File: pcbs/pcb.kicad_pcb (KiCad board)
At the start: 2 copper layers, 148.3 x 111.7 mm, 54 parts

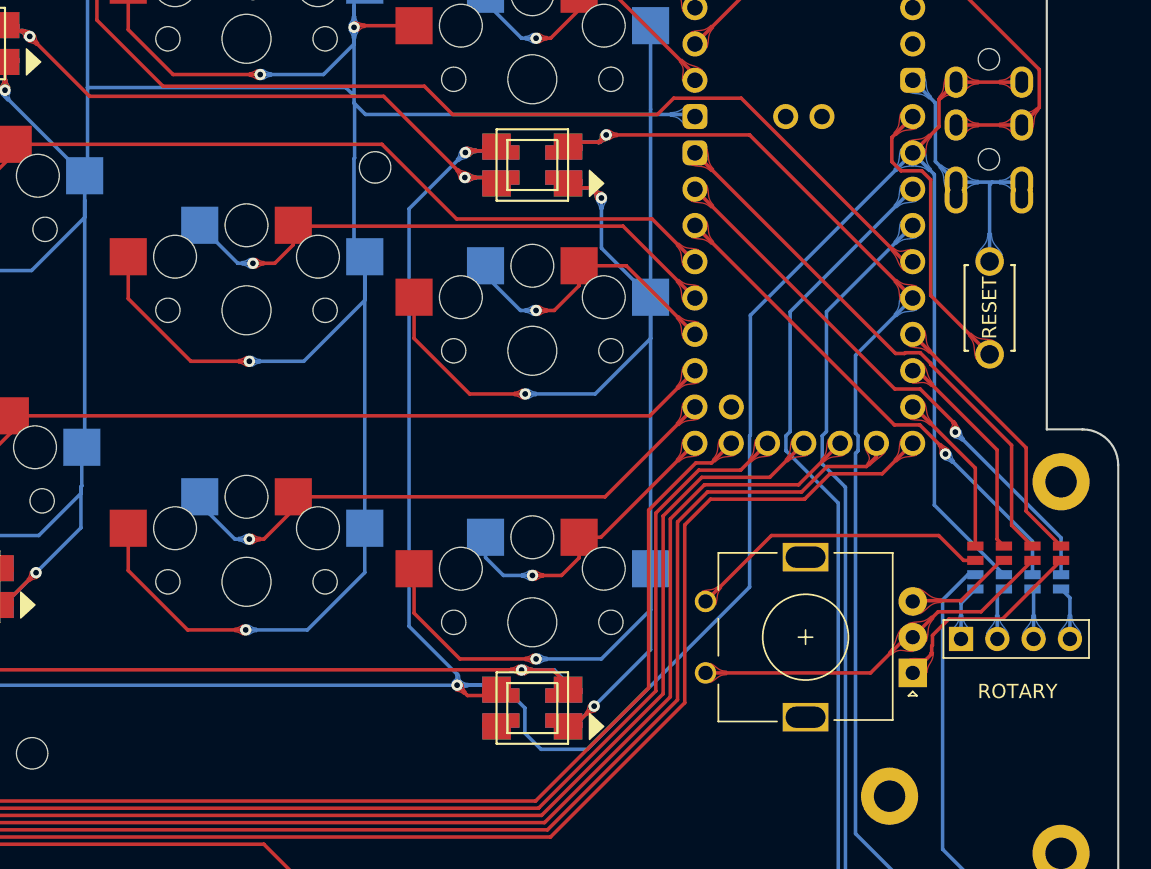
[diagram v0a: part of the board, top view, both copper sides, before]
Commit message: Connect LEDs' VDD pin to Helios' RGB pin for stable 5V
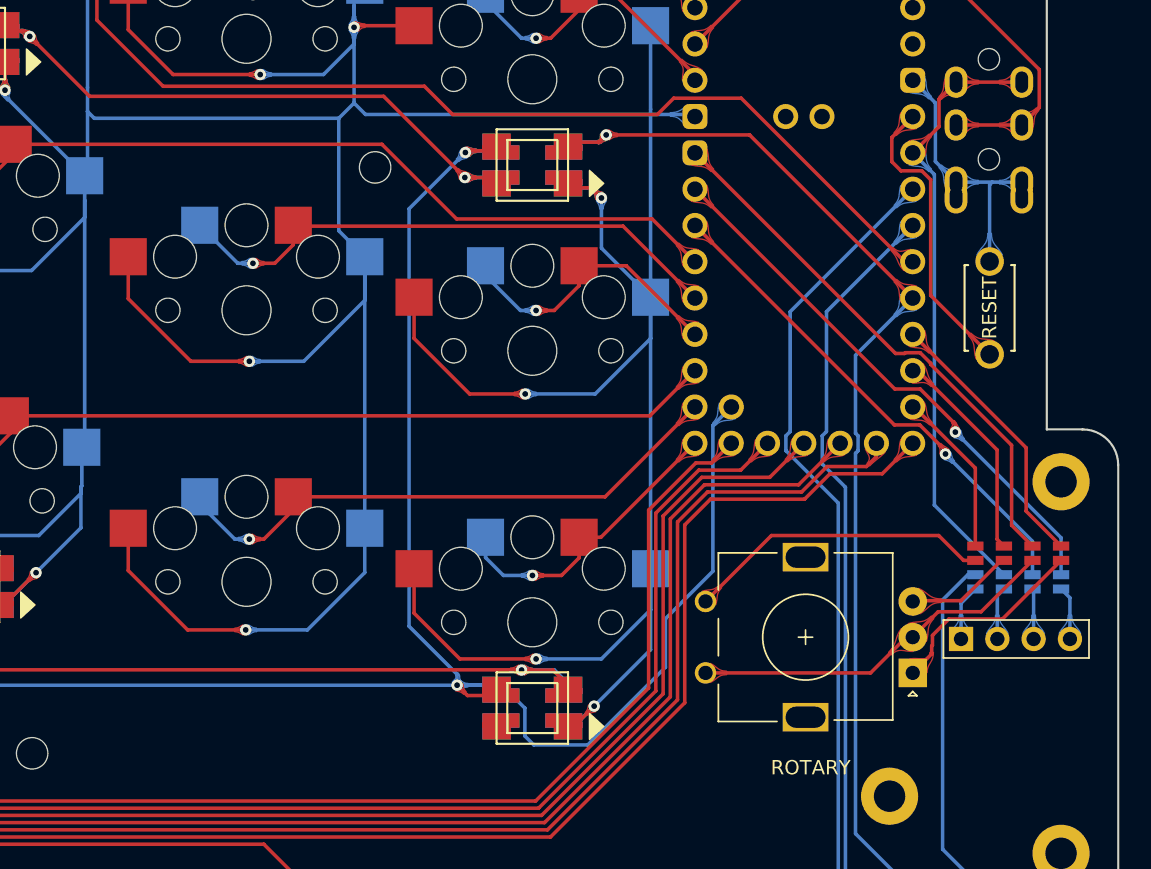
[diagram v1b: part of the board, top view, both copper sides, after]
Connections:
- LED1 pad 1: VCC -> RGB
- LED1 pad 11: VCC -> RGB
- LED10 pad 1: VCC -> RGB
- LED10 pad 11: VCC -> RGB
- LED11 pad 1: VCC -> RGB
- LED11 pad 11: VCC -> RGB
- LED12 pad 1: VCC -> RGB
- LED12 pad 11: VCC -> RGB
- LED2 pad 1: VCC -> RGB
- LED2 pad 11: VCC -> RGB
- LED3 pad 1: VCC -> RGB
- LED3 pad 11: VCC -> RGB
- LED4 pad 1: VCC -> RGB
- LED4 pad 11: VCC -> RGB
- LED5 pad 1: VCC -> RGB
- LED5 pad 11: VCC -> RGB
- LED6 pad 1: VCC -> RGB
- LED6 pad 11: VCC -> RGB
- LED7 pad 1: VCC -> RGB
- LED7 pad 11: VCC -> RGB
- LED8 pad 1: VCC -> RGB
- LED8 pad 11: VCC -> RGB
- LED9 pad 1: VCC -> RGB
- LED9 pad 11: VCC -> RGB
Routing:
- net VCC: track 332.6 -> 43.0 mm, vias 6 -> 0
- net RGB: track 0.00 -> 265.7 mm, vias 0 -> 6

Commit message: Add support for azoteq TPS43 while maintaining support for cirque
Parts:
- removed the ? at (153.4, 156.2) (x4)
- removed CIRQUE: VAL**, CIRQUE-TM040040
- added ?: LOGO, Library:fractalx, B.Cu at (36.1, 13.5)
- added ?: , Azoteq-TPS45, F.Cu at (138.0, -30.5)
- added ?: LOGO, Library:fractalx, F.Cu at (36.1, 13.5)
- added ?: LOGO, Library:fractalxcu, F.Cu at (36.1, 13.5)
- added ?: LOGO, Library:fractalxcu, B.Cu at (36.1, 13.5)
- added ?: , Resistor_SMD:R_0805_2012Metric_Pad1.20x1.40mm_HandSolder, B.Cu at (114.0, 1.00)
- added ?: , Resistor_SMD:R_0805_2012Metric_Pad1.20x1.40mm_HandSolder, B.Cu at (114.0, -5.00)
- added ?: , Resistor_SMD:R_0805_2012Metric_Pad1.20x1.40mm_HandSolder, B.Cu at (114.0, 4.00)
- added ?: , Resistor_SMD:R_0805_2012Metric_Pad1.20x1.40mm_HandSolder, B.Cu at (114.0, -2.00)
- added J10: , lib:Jumper, F.Cu at (121.0, -12.0)
- added J9: , lib:Jumper, F.Cu at (119.0, -12.0)
- ?: renamed from O2; value TRACKPAD -> (none)
- moved S18 188.3 mm to (111.5, 34.3)
- moved S17 187.1 mm to (92.6, 26.3)
- moved S16 186.5 mm to (72.0, 22.8)
- moved ? 180.3 mm to (110.0, -8.00)
- moved J1 180.3 mm to (111.0, -14.0)
- moved J2 180.3 mm to (113.0, -14.0)
- moved J3 180.3 mm to (115.0, -14.0)
- moved J4 180.3 mm to (117.0, -14.0)
- moved J5 180.3 mm to (111.0, -12.0)
- moved J6 180.3 mm to (113.0, -12.0)
- moved J7 180.3 mm to (115.0, -12.0)
- moved J8 180.3 mm to (117.0, -12.0)
- moved LED1 180.3 mm to (20.0, -44.0)
- moved LED11 180.3 mm to (80.0, -41.2)
- moved LED12 180.3 mm to (80.0, -3.17)
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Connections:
- LED11 pad 4: A0 -> A1
- LED11 pad 44: A0 -> A1
- LED5 pad 4: A0 -> A1
- LED5 pad 44: A0 -> A1
- S9 pad 1: A1 -> IO11
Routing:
- net IO11: track 0.00 -> 86.9 mm, vias 0 -> 1
- net A1: track 88.7 -> 31.5 mm
- net GND: track 965.6 -> 922.6 mm
- net A0: track 111.8 -> 74.9 mm, vias 2 -> 1
- net T6: track 0.00 -> 19.4 mm
- net IO20: track 15.1 -> 33.5 mm, vias 0 -> 1
- net IO23: track 11.6 -> 29.5 mm, vias 0 -> 1
- net T5: track 0.00 -> 15.2 mm
- net T2: track 3.69 -> 15.9 mm
- net A3: track 88.9 -> 97.4 mm
- net RGB: track 265.7 -> 273.2 mm
- net T4: track 3.76 -> 10.8 mm
- net A2: track 69.2 -> 74.0 mm
- net T3: track 3.53 -> 6.57 mm
- net IO10: track 39.2 -> 40.6 mm
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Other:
- board size 148.3 x 111.7 mm -> 136 x 112 mm
- board text removed: "ROTARY"
- board text removed: "TRACKPAD"
